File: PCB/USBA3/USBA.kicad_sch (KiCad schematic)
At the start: 20 parts, among them J1 USB_A, U1 ESP32-PICO-MINI-02, U2 Barcode, U3 CH340X, U4 QR, U5 MD8942, U7 SHT40

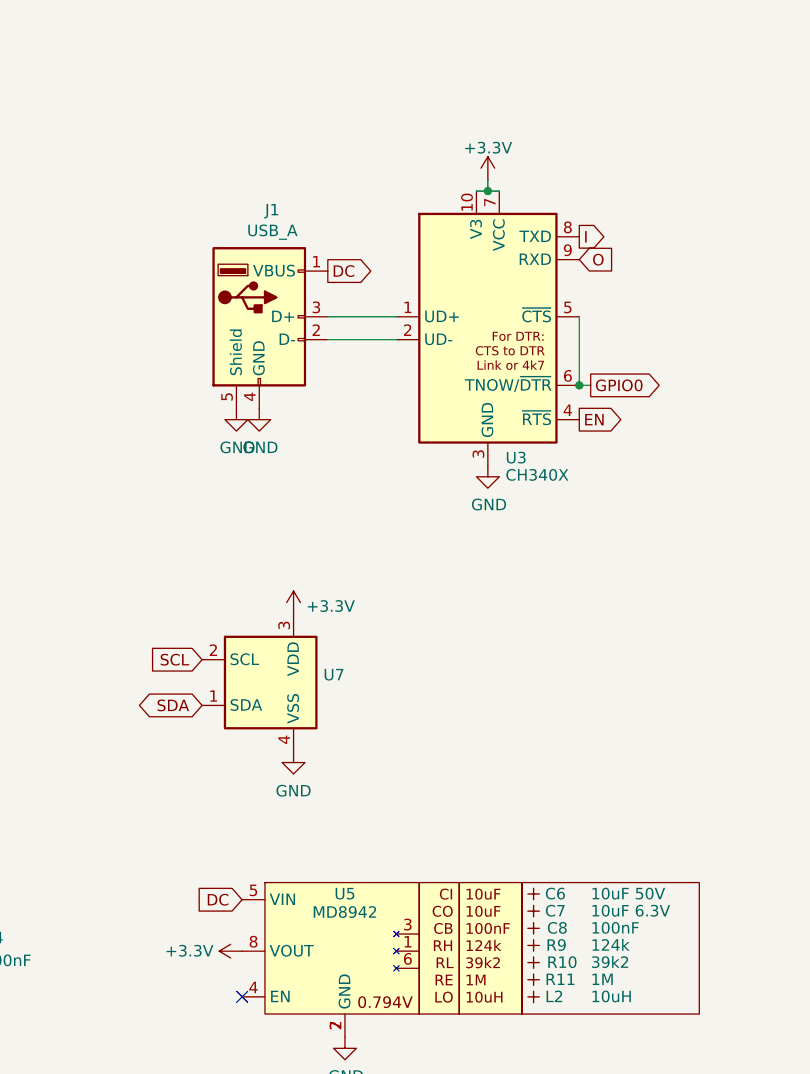
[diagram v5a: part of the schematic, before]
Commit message: Started rework for single sided
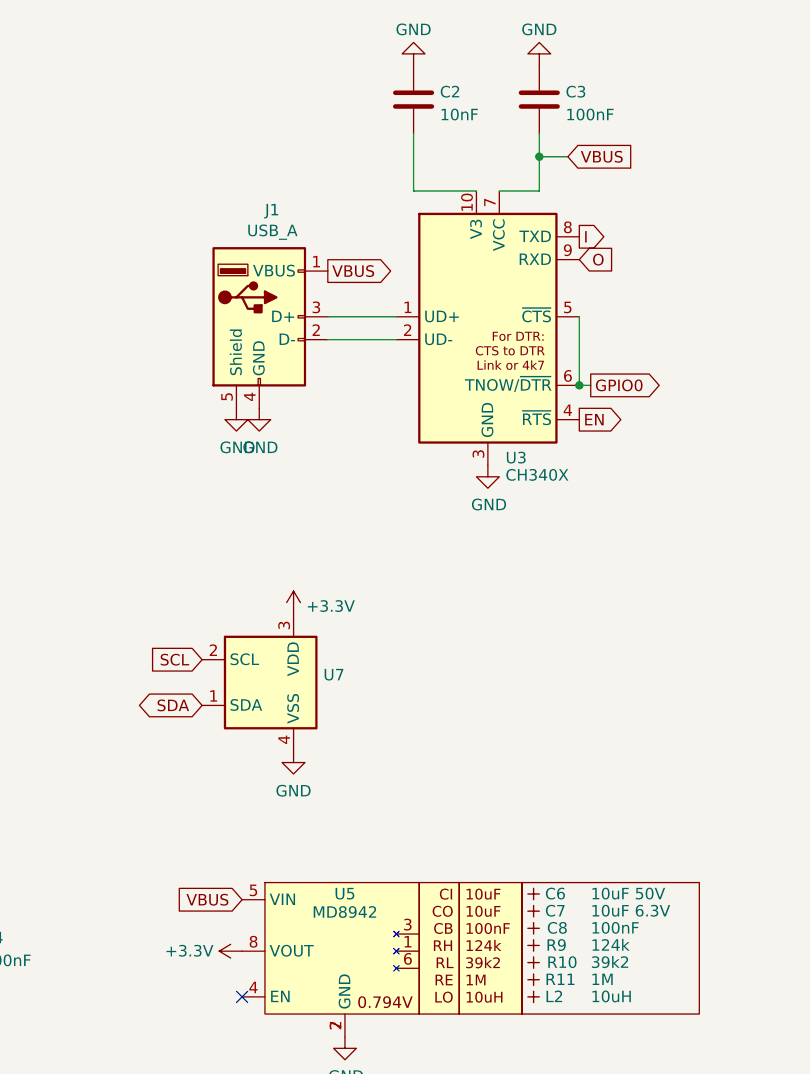
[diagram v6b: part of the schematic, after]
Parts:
- added C2: 10nF, RevK:C_0402, symbol Device:C
- added C3: 100nF, RevK:C_0402, symbol Device:C
- added V1, V2: 70, RevK:VCUT70, symbol RevK:VCUT
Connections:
- net +3.3V: no longer U3.10 (V3), U3.7 (VCC)
- net GND: now also C2.1, C3.1
- net DC renamed VBUS
- net VBUS: now also U3.7 (VCC), C3.2
- new net: C2.2, U3.10 (V3)
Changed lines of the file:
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@@
     (comment 2 "www.me.uk")
   )
-  (junction (at 193.04 43.18) (diameter 0) (color 0 0 0 0)
-  )
   (junction (at 203.2 64.77) (diameter 0) (color 0 0 0 0)
+  )
+  (junction (at 198.755 39.37) (diameter 0) (color 0 0 0 0)
   )
   (no_connect (at 121.92 80.01))
@@
     (stroke (width 0) (type default))
   )
+  (wire (pts (xy 198.755 36.83) (xy 198.755 39.37))
+    (stroke (width 0) (type default))
+  )
   (wire (pts (xy 121.92 58.42) (xy 124.46 58.42))
     (stroke (width 0) (type default))
   )
-  (wire (pts (xy 191.77 43.18) (xy 193.04 43.18))
+  (wire (pts (xy 201.93 39.37) (xy 198.755 39.37))
     (stroke (width 0) (type default))
   )
@@
     (stroke (width 0) (type default))
   )
-  (wire (pts (xy 193.04 43.18) (xy 194.31 43.18))
+  (wire (pts (xy 194.31 43.18) (xy 198.755 43.18))
     (stroke (width 0) (type default))
   )
@@
     (stroke (width 0) (type default))
   )
+  (wire (pts (xy 184.785 43.18) (xy 191.77 43.18))
+    (stroke (width 0) (type default))
+  )
   (wire (pts (xy 203.2 64.77) (xy 204.47 64.77))
     (stroke (width 0) (type default))
   )
-  (wire (pts (xy 193.04 41.91) (xy 193.04 43.18))
+  (wire (pts (xy 184.785 36.83) (xy 184.785 43.18))
+    (stroke (width 0) (type default))
+  )
+  (wire (pts (xy 198.755 39.37) (xy 198.755 43.18))
     (stroke (width 0) (type default))
   )
@@
     )
   )
-  (global_label "DC" (shape input) (at 165.735 121.92 180) (fields_autoplaced)
+  (global_label "VBUS" (shape input) (at 165.735 121.92 180) (fields_autoplaced)
     (effects (font (size 1.27 1.27)) (justify right))
-    (property "Intersheetrefs" "${INTERSHEET_REFS}" (at 160.9434 121.92 0)
+    (property "Intersheetrefs" "${INTERSHEET_REFS}" (at 158.5848 121.92 0)
       (effects (font (size 1.27 1.27)) (justify right) hide)
     )
@@
     )
   )
+  (global_label "VBUS" (shape input) (at 201.93 39.37 0) (fields_autoplaced)
+    (effects (font (size 1.27 1.27)) (justify left))
+    (property "Intersheetrefs" "${INTERSHEET_REFS}" (at 209.0802 39.37 0)
+      (effects (font (size 1.27 1.27)) (justify left) hide)
+    )
+  )
   (global_label "O" (shape input) (at 203.2 50.8 0) (fields_autoplaced)
     (effects (font (size 1.27 1.27)) (justify left))
@@
     )
   )
-  (global_label "DC" (shape output) (at 175.26 52.07 0) (fields_autoplaced)
+  (global_label "VBUS" (shape output) (at 175.26 52.07 0) (fields_autoplaced)
     (effects (font (size 1.27 1.27)) (justify left))
-    (property "Intersheetrefs" "${INTERSHEET_REFS}" (at 180.1242 51.9906 0)
+    (property "Intersheetrefs" "${INTERSHEET_REFS}" (at 182.4102 52.07 0)
       (effects (font (size 1.27 1.27)) (justify left) hide)
     )
@@
     )
   )
+  (symbol (lib_id "Device:C") (at 198.755 33.02 0) (unit 1)
+    (in_bom yes) (on_board yes) (dnp no) (fields_autoplaced)
+    (property "Reference" "C3" (at 201.676 32.1853 0)
+      (effects (font (size 1.27 1.27)) (justify left))
+    )
+    (property "Value" "100nF" (at 201.676 34.7222 0)
+      (effects (font (size 1.27 1.27)) (justify left))
+    )
+    (property "Footprint" "RevK:C_0402" (at 199.7202 36.83 0)
+      (effects (font (size 1.27 1.27)) hide)
+    )
+    (property "Datasheet" "~" (at 198.755 33.02 0)
+      (effects (font (size 1.27 1.27)) hide)
+    )
+    (pin "1")
+    (pin "2")
+    (instances
+      (project "USBA"
+        (path "/2d210a96-f81f-42a9-8bf4-1b43c11086f3"
+          (reference "C3") (unit 1)
+        )
+      )
+      (project "Tas"
+        (path "/42713045-fffd-4b2d-ae1e-7232d705fb12"
+          (reference "C3") (unit 1)
+        )
+      )
+    )
+  )
   (symbol (lib_id "RevK:SHT40") (at 168.91 97.79 0) (unit 1)
     (in_bom yes) (on_board yes) (dnp no) (fields_autoplaced)
@@
         (path "/825c70b0-4860-42b7-97dc-86bfa46e06fd"
           (reference "D2") (unit 1)
+        )
+      )
+    )
+  )
+  (symbol (lib_id "RevK:VCUT") (at 250.19 175.895 0) (unit 1)
+    (in_bom no) (on_board yes) (dnp no) (fields_autoplaced)
+    (property "Reference" "V2" (at 250.19 174.625 0)
+      (effects (font (size 1.27 1.27)) hide)
+    )
+    (property "Value" "70" (at 244.475 175.895 0)
+      (effects (font (size 1.27 1.27)) hide)
+    )
+    (property "Footprint" "RevK:VCUT70" (at 250.19 177.165 0)
+      (effects (font (size 1.27 1.27)) hide)
+    )
+    (property "Datasheet" "" (at 250.19 175.895 0)
+      (effects (font (size 1.27 1.27)) hide)
+    )
+    (property "Sim.Enable" "0" (at 250.19 175.895 0)
+      (effects (font (size 1.27 1.27)) hide)
+    )
+    (instances
+      (project "USBA"
+        (path "/2d210a96-f81f-42a9-8bf4-1b43c11086f3"
+          (reference "V2") (unit 1)
         )
       )
@@
         (path "/2d210a96-f81f-42a9-8bf4-1b43c11086f3"
           (reference "#PWR0102") (unit 1)
+        )
+      )
+    )
+  )
+  (symbol (lib_id "RevK:VCUT") (at 250.19 169.545 0) (unit 1)
+    (in_bom no) (on_board yes) (dnp no) (fields_autoplaced)
+    (property "Reference" "V1" (at 250.19 168.275 0)
+      (effects (font (size 1.27 1.27)) hide)
+    )
+    (property "Value" "70" (at 244.475 169.545 0)
+      (effects (font (size 1.27 1.27)) hide)
+    )
+    (property "Footprint" "RevK:VCUT70" (at 250.19 170.815 0)
+      (effects (font (size 1.27 1.27)) hide)
+    )
+    (property "Datasheet" "" (at 250.19 169.545 0)
+      (effects (font (size 1.27 1.27)) hide)
+    )
+    (property "Sim.Enable" "0" (at 250.19 169.545 0)
+      (effects (font (size 1.27 1.27)) hide)
+    )
+    (instances
+      (project "USBA"
+        (path "/2d210a96-f81f-42a9-8bf4-1b43c11086f3"
+          (reference "V1") (unit 1)
         )
       )
@@
     )
   )
-  (symbol (lib_id "power:+3.3V") (at 193.04 41.91 0) (unit 1)
-    (in_bom yes) (on_board yes) (dnp no) (fields_autoplaced)
-    (property "Reference" "#PWR03" (at 193.04 45.72 0)
-      (effects (font (size 1.27 1.27)) hide)
-    )
-    (property "Value" "+3.3V" (at 193.04 38.4081 0)
-      (effects (font (size 1.27 1.27)))
-    )
-    (property "Footprint" "" (at 193.04 41.91 0)
-      (effects (font (size 1.27 1.27)) hide)
-    )
-    (property "Datasheet" "" (at 193.04 41.91 0)
-      (effects (font (size 1.27 1.27)) hide)
-    )
-    (pin "1")
-    (instances
-      (project "USBA"
-        (path "/2d210a96-f81f-42a9-8bf4-1b43c11086f3"
-          (reference "#PWR03") (unit 1)
-        )
-      )
-    )
-  )
   (symbol (lib_id "RevK:PCB") (at 250.19 172.72 0) (unit 1)
     (in_bom no) (on_board yes) (dnp no)
@@
     )
   )
+  (symbol (lib_id "Device:C") (at 184.785 33.02 0) (unit 1)
+    (in_bom yes) (on_board yes) (dnp no) (fields_autoplaced)
+    (property "Reference" "C2" (at 187.706 32.1853 0)
+      (effects (font (size 1.27 1.27)) (justify left))
+    )
+    (property "Value" "10nF" (at 187.706 34.7222 0)
+      (effects (font (size 1.27 1.27)) (justify left))
+    )
+    (property "Footprint" "RevK:C_0402" (at 185.7502 36.83 0)
+      (effects (font (size 1.27 1.27)) hide)
+    )
+    (property "Datasheet" "~" (at 184.785 33.02 0)
+      (effects (font (size 1.27 1.27)) hide)
+    )
+    (pin "1")
+    (pin "2")
+    (instances
+      (project "USBA"
+        (path "/2d210a96-f81f-42a9-8bf4-1b43c11086f3"
+          (reference "C2") (unit 1)
+        )
+      )
+      (project "Tas"
+        (path "/42713045-fffd-4b2d-ae1e-7232d705fb12"
+          (reference "C2") (unit 1)
+        )
+      )
+    )
+  )
+  (symbol (lib_id "power:GND") (at 184.785 29.21 180) (unit 1)
+    (in_bom yes) (on_board yes) (dnp no) (fields_autoplaced)
+    (property "Reference" "#PWR08" (at 184.785 22.86 0)
+      (effects (font (size 1.27 1.27)) hide)
+    )
+    (property "Value" "GND" (at 184.785 25.265 0)
+      (effects (font (size 1.27 1.27)))
+    )
+    (property "Footprint" "" (at 184.785 29.21 0)
+      (effects (font (size 1.27 1.27)) hide)
+    )
+    (property "Datasheet" "" (at 184.785 29.21 0)
+      (effects (font (size 1.27 1.27)) hide)
+    )
+    (pin "1")
+    (instances
+      (project "USBA"
+        (path "/2d210a96-f81f-42a9-8bf4-1b43c11086f3"
+          (reference "#PWR08") (unit 1)
+        )
+      )
+      (project "Tas"
+        (path "/42713045-fffd-4b2d-ae1e-7232d705fb12"
+          (reference "#PWR08") (unit 1)
+        )
+      )
+    )
+  )
   (symbol (lib_id "Device:C") (at 133.985 127 0) (unit 1)
     (in_bom yes) (on_board yes) (dnp no) (fields_autoplaced)
@@
         )
       )
+    )
+  )
+  (symbol (lib_id "power:GND") (at 198.755 29.21 180) (unit 1)
+    (in_bom yes) (on_board yes) (dnp no) (fields_autoplaced)
+    (property "Reference" "#PWR011" (at 198.755 22.86 0)
+      (effects (font (size 1.27 1.27)) hide)
+    )
+    (property "Value" "GND" (at 198.755 25.265 0)
+      (effects (font (size 1.27 1.27)))
+    )
+    (property "Footprint" "" (at 198.755 29.21 0)
+      (effects (font (size 1.27 1.27)) hide)
+    )
+    (property "Datasheet" "" (at 198.755 29.21 0)
+      (effects (font (size 1.27 1.27)) hide)
+    )
+    (pin "1")
+    (instances
+      (project "USBA"
+        (path "/2d210a96-f81f-42a9-8bf4-1b43c11086f3"
+          (reference "#PWR011") (unit 1)
+        )
+      )
+      (project "Tas"
+        (path "/42713045-fffd-4b2d-ae1e-7232d705fb12"
+          (reference "#PWR023") (unit 1)
+        )
+      )

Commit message: New layout
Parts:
- added C1: 22uF, RevK:C_0402, symbol Device:C
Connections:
- net GND: now also C1.1
- net VBUS: now also C1.2
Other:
- moved on the sheet: C3
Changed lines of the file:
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@@
     (comment 2 "www.me.uk")
   )
+  (junction (at 207.645 38.735) (diameter 0) (color 0 0 0 0)
+  )
   (junction (at 203.2 64.77) (diameter 0) (color 0 0 0 0)
   )
-  (junction (at 198.755 39.37) (diameter 0) (color 0 0 0 0)
+  (junction (at 201.295 38.735) (diameter 0) (color 0 0 0 0)
   )
   (no_connect (at 121.92 80.01))
@@
     (stroke (width 0) (type default))
   )
-  (wire (pts (xy 198.755 36.83) (xy 198.755 39.37))
-    (stroke (width 0) (type default))
-  )
   (wire (pts (xy 121.92 58.42) (xy 124.46 58.42))
     (stroke (width 0) (type default))
   )
-  (wire (pts (xy 201.93 39.37) (xy 198.755 39.37))
+  (wire (pts (xy 207.645 38.735) (xy 210.82 38.735))
+    (stroke (width 0) (type default))
+  )
+  (wire (pts (xy 207.645 36.83) (xy 207.645 38.735))
+    (stroke (width 0) (type default))
+  )
+  (wire (pts (xy 201.295 38.735) (xy 201.295 43.18))
     (stroke (width 0) (type default))
   )
@@
     (stroke (width 0) (type default))
   )
+  (wire (pts (xy 201.295 36.83) (xy 201.295 38.735))
+    (stroke (width 0) (type default))
+  )
   (wire (pts (xy 121.92 53.34) (xy 123.825 53.34))
     (stroke (width 0) (type default))
   )
-  (wire (pts (xy 194.31 43.18) (xy 198.755 43.18))
+  (wire (pts (xy 194.31 43.18) (xy 201.295 43.18))
+    (stroke (width 0) (type default))
+  )
+  (wire (pts (xy 201.295 38.735) (xy 207.645 38.735))
     (stroke (width 0) (type default))
   )
@@
   )
   (wire (pts (xy 184.785 36.83) (xy 184.785 43.18))
-    (stroke (width 0) (type default))
-  )
-  (wire (pts (xy 198.755 39.37) (xy 198.755 43.18))
     (stroke (width 0) (type default))
   )
@@
     )
   )
-  (global_label "VBUS" (shape input) (at 201.93 39.37 0) (fields_autoplaced)
+  (global_label "VBUS" (shape input) (at 210.82 38.735 0) (fields_autoplaced)
     (effects (font (size 1.27 1.27)) (justify left))
-    (property "Intersheetrefs" "${INTERSHEET_REFS}" (at 209.0802 39.37 0)
+    (property "Intersheetrefs" "${INTERSHEET_REFS}" (at 217.9702 38.735 0)
       (effects (font (size 1.27 1.27)) (justify left) hide)
     )
@@
     )
   )
-  (symbol (lib_id "Device:C") (at 198.755 33.02 0) (unit 1)
-    (in_bom yes) (on_board yes) (dnp no) (fields_autoplaced)
-    (property "Reference" "C3" (at 201.676 32.1853 0)
-      (effects (font (size 1.27 1.27)) (justify left))
-    )
-    (property "Value" "100nF" (at 201.676 34.7222 0)
-      (effects (font (size 1.27 1.27)) (justify left))
-    )
-    (property "Footprint" "RevK:C_0402" (at 199.7202 36.83 0)
-      (effects (font (size 1.27 1.27)) hide)
-    )
-    (property "Datasheet" "~" (at 198.755 33.02 0)
+  (symbol (lib_id "Device:C") (at 201.295 33.02 0) (unit 1)
+    (in_bom yes) (on_board yes) (dnp no)
+    (property "Reference" "C3" (at 193.675 33.6581 0)
+      (effects (font (size 1.27 1.27)) (justify left))
+    )
+    (property "Value" "100nF" (at 193.675 36.195 0)
+      (effects (font (size 1.27 1.27)) (justify left))
+    )
+    (property "Footprint" "RevK:C_0402" (at 202.2602 36.83 0)
+      (effects (font (size 1.27 1.27)) hide)
+    )
+    (property "Datasheet" "~" (at 201.295 33.02 0)
       (effects (font (size 1.27 1.27)) hide)
     )
@@
         (path "/2d210a96-f81f-42a9-8bf4-1b43c11086f3"
           (reference "#PWR0106") (unit 1)
+        )
+      )
+    )
+  )
+  (symbol (lib_id "power:GND") (at 207.645 29.21 180) (unit 1)
+    (in_bom yes) (on_board yes) (dnp no) (fields_autoplaced)
+    (property "Reference" "#PWR03" (at 207.645 22.86 0)
+      (effects (font (size 1.27 1.27)) hide)
+    )
+    (property "Value" "GND" (at 207.645 25.265 0)
+      (effects (font (size 1.27 1.27)))
+    )
+    (property "Footprint" "" (at 207.645 29.21 0)
+      (effects (font (size 1.27 1.27)) hide)
+    )
+    (property "Datasheet" "" (at 207.645 29.21 0)
+      (effects (font (size 1.27 1.27)) hide)
+    )
+    (pin "1")
+    (instances
+      (project "USBA"
+        (path "/2d210a96-f81f-42a9-8bf4-1b43c11086f3"
+          (reference "#PWR03") (unit 1)
+        )
+      )
+      (project "Tas"
+        (path "/42713045-fffd-4b2d-ae1e-7232d705fb12"
+          (reference "#PWR023") (unit 1)
         )
       )
@@
     )
   )
+  (symbol (lib_id "Device:C") (at 207.645 33.02 0) (unit 1)
+    (in_bom yes) (on_board yes) (dnp no)
+    (property "Reference" "C1" (at 211.455 33.02 0)
+      (effects (font (size 1.27 1.27)) (justify left))
+    )
+    (property "Value" "22uF" (at 211.455 35.5569 0)
+      (effects (font (size 1.27 1.27)) (justify left))
+    )
+    (property "Footprint" "RevK:C_0402" (at 208.6102 36.83 0)
+      (effects (font (size 1.27 1.27)) hide)
+    )
+    (property "Datasheet" "~" (at 207.645 33.02 0)
+      (effects (font (size 1.27 1.27)) hide)
+    )
+    (pin "1")
+    (pin "2")
+    (instances
+      (project "USBA"
+        (path "/2d210a96-f81f-42a9-8bf4-1b43c11086f3"
+          (reference "C1") (unit 1)
+        )
+      )
+      (project "Tas"
+        (path "/42713045-fffd-4b2d-ae1e-7232d705fb12"
+          (reference "C3") (unit 1)
+        )
+      )
+    )
+  )
   (symbol (lib_id "RevK:Hidden") (at 198.12 127 0) (unit 1)
     (in_bom yes) (on_board yes) (dnp no)
@@
   )
   (symbol (lib_id "Device:C") (at 184.785 33.02 0) (unit 1)
-    (in_bom yes) (on_board yes) (dnp no) (fields_autoplaced)
-    (property "Reference" "C2" (at 187.706 32.1853 0)
-      (effects (font (size 1.27 1.27)) (justify left))
-    )
-    (property "Value" "10nF" (at 187.706 34.7222 0)
+    (in_bom yes) (on_board yes) (dnp no)
+    (property "Reference" "C2" (at 179.07 34.2931 0)
+      (effects (font (size 1.27 1.27)) (justify left))
+    )
+    (property "Value" "10nF" (at 179.07 36.83 0)
       (effects (font (size 1.27 1.27)) (justify left))
     )
@@
     )
   )
-  (symbol (lib_id "power:GND") (at 198.755 29.21 180) (unit 1)
+  (symbol (lib_id "power:GND") (at 201.295 29.21 180) (unit 1)
     (in_bom yes) (on_board yes) (dnp no) (fields_autoplaced)
-    (property "Reference" "#PWR011" (at 198.755 22.86 0)
-      (effects (font (size 1.27 1.27)) hide)
-    )
-    (property "Value" "GND" (at 198.755 25.265 0)
-      (effects (font (size 1.27 1.27)))
-    )
-    (property "Footprint" "" (at 198.755 29.21 0)
-      (effects (font (size 1.27 1.27)) hide)
-    )
-    (property "Datasheet" "" (at 198.755 29.21 0)
-      (effects (font (size 1.27 1.27)) hide)
-    )
+    (property "Reference" "#PWR011" (at 201.295 22.86 0)
+      (effects (font (size 1.27 1.27)) hide)
+    )
+    (property "Value" "GND" (at 201.295 25.265 0)
+      (effects (font (size 1.27 1.27)))
+    )
+    (property "Footprint" "" (at 201.295 29.21 0)
+      (effects (font (size 1.27 1.27)) hide)
+    )
+    (property "Datasheet" "" (at 201.295 29.21 0)
+      (effects (font (size 1.27 1.27)) hide)
+    )

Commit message: 1mm with glued bits
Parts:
- removed U2: Barcode, RevK:EAN-5060634238069, symbol RevK:Barcode
- removed U4: QR, RevK:QR-USBA, symbol RevK:QR
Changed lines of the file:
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@@
-    )
-  )
-  (symbol (lib_id "RevK:QR") (at 264.16 172.085 0) (unit 1)
-    (in_bom no) (on_board yes) (dnp no)
-    (property "Reference" "U4" (at 264.16 175.26 0)
-      (effects (font (size 1.27 1.27)) hide)
-    )
-    (property "Value" "QR" (at 264.16 175.26 0)
-      (effects (font (size 1.27 1.27)) hide)
-    )
-    (property "Footprint" "RevK:QR-USBA" (at 263.525 172.72 0)
-      (effects (font (size 1.27 1.27)) hide)
-    )
-    (property "Datasheet" "" (at 263.525 172.72 0)
-      (effects (font (size 1.27 1.27)) hide)
-    )
-    (property "Note" "Non part, PCB printed" (at 264.16 172.085 0)
-      (effects (font (size 1.27 1.27)) hide)
-    )
-    (instances
-      (project "USBA"
-        (path "/2d210a96-f81f-42a9-8bf4-1b43c11086f3"
-          (reference "U4") (unit 1)
-        )
-      )
     )
   )
@@
         )
       )
-    )
-  )
-  (symbol (lib_id "RevK:Barcode") (at 271.145 172.085 0) (unit 1)
-    (in_bom no) (on_board yes) (dnp no) (fields_autoplaced)
-    (property "Reference" "U2" (at 271.145 175.26 0)
-      (effects (font (size 1.27 1.27)) hide)
-    )
-    (property "Value" "Barcode" (at 271.145 177.165 0)
-      (effects (font (size 1.27 1.27)) hide)
-    )
-    (property "Footprint" "RevK:EAN-5060634238069" (at 270.51 172.72 0)
-      (effects (font (size 1.27 1.27)) hide)
-    )
-    (property "Datasheet" "" (at 270.51 172.72 0)
-      (effects (font (size 1.27 1.27)) hide)
-    )
-    (property "Note" "Non part, PCB printed" (at 271.145 166.37 0)
-      (effects (font (size 1.27 1.27)) hide)
-    )
-    (instances
-      (project "USBA"
-        (path "/2d210a96-f81f-42a9-8bf4-1b43c11086f3"
-          (reference "U2") (unit 1)
-        )
-      )
-      (project "Faikin"
-        (path "/46c350bb-7de4-4e81-aafd-4af55e37aab0"
-          (reference "U4") (unit 1)
-        )
-      )
